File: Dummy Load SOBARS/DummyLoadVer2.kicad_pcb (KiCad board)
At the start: 2 copper layers, 57.2 x 47.6 mm, 22 parts, among them J2 Batt Monitor, J4 To Dummy Load 50 Ohms

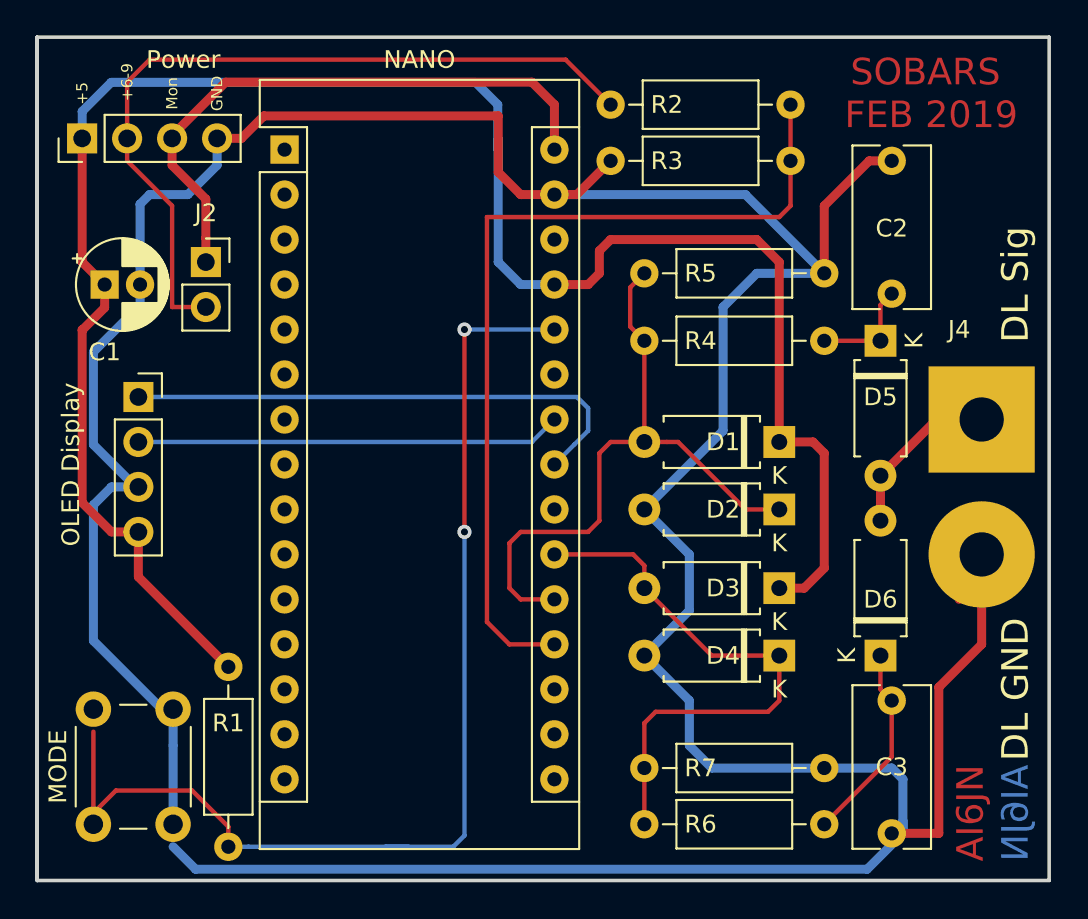
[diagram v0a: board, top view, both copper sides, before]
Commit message: Fix Mode Pin Digital Minor adjustments
Clean up some traces
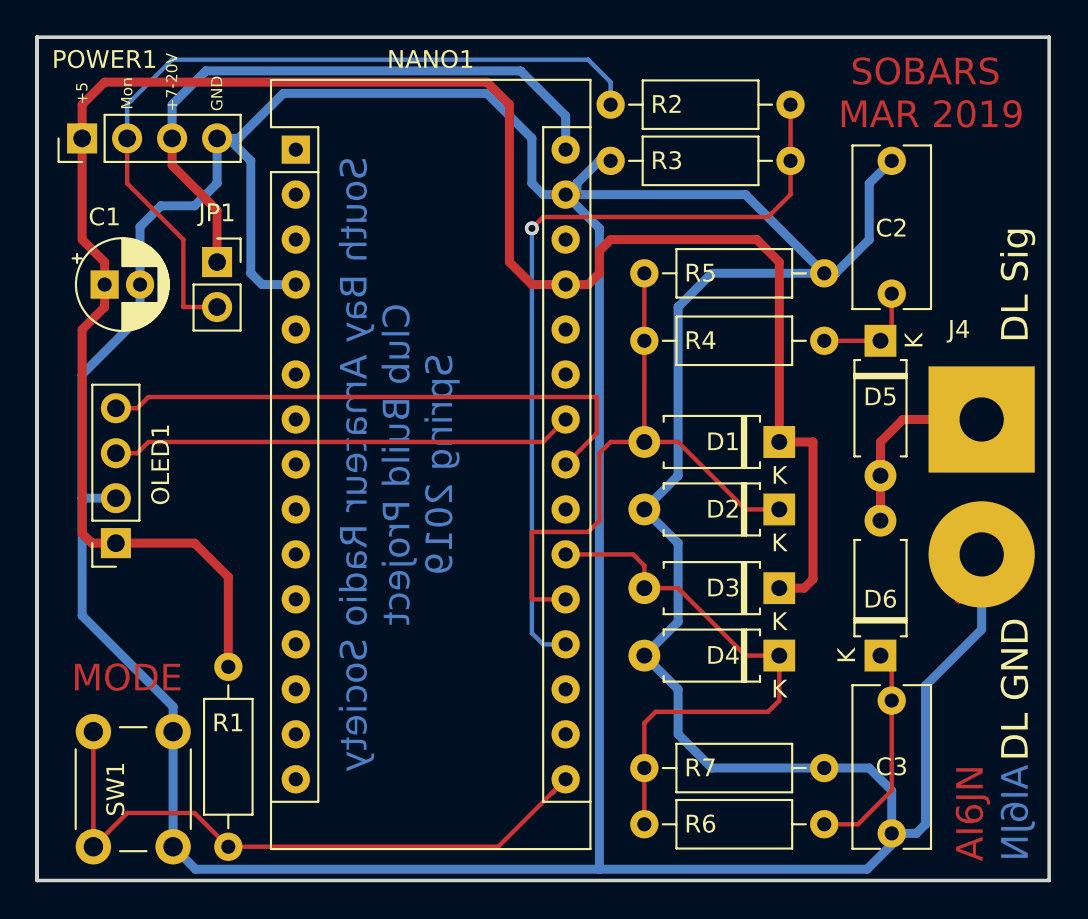
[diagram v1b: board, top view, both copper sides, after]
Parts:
- removed J2: Batt Monitor, Connector_PinSocket_2.54mm:PinSocket_1x02_P2.54mm_Vertical
- removed MODE: SW1, Button_Switch_THT:SW_PUSH_6mm
- removed NANO: Arduino_Nano_v3.x, Module:Arduino_Nano
- removed OLED Display: OLED Display 128X64, Connector_PinSocket_2.54mm:PinSocket_1x04_P2.54mm_Vertical
- removed Power: Power, Connector_PinHeader_2.54mm:PinHeader_1x04_P2.54mm_Vertical
- added JP1: Monitor Select, Connector_PinSocket_2.54mm:PinSocket_1x02_P2.54mm_Vertical, F.Cu at (76.8, 43.2)
- added NANO1: Arduino_Nano_v3.x, Module:Arduino_Nano, F.Cu at (81.3, 36.8)
- added OLED1: OLED Display 128X64, Connector_PinSocket_2.54mm:PinSocket_1x04_P2.54mm_Vertical, F.Cu at (71.1, 59.1)
- added POWER1: Power, Connector_PinHeader_2.54mm:PinHeader_1x04_P2.54mm_Vertical, F.Cu at (69.2, 36.2)
- added SW1: MODE, Button_Switch_THT:SW_PUSH_6mm, F.Cu at (69.8, 76.2)
- C1: value 4.7 -> 4.7uF
- C2, C3: value CAP -> 0.022uF
- J4: value To Dummy Load 50 Ohms -> To Dummy Load 50 Ohms
- R2: value 50K -> 22K
- R3: value 50K -> 6.8K
- R5: value 9K -> 8.2K
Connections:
- net Net-(D1-Pad2) renamed /LowADC
- net Net-(D3-Pad2) renamed /HighADC
- net Net-(D5-Pad2) renamed /LoadPositive
- net Net-(NANO1-Pad19) renamed /BattADC
- R1 pad 2: Net-(MODE1-Pad1) -> /MODE
- R2 pad 1: Net-(J1-Pad2) -> /BattMon
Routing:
- net Net-(MODE1-Pad1): track 63.2 -> 0.00 mm, vias 2 -> 0
- net GND: track 219.5 -> 270.3 mm
- net Net-(J1-Pad2): track 44.5 -> 0.00 mm
- net /BattMon: track 0.00 -> 44.2 mm
- net /MODE: track 0.00 -> 38.1 mm
- net /VinUnReg: track 0.00 -> 36.1 mm
- net Net-(J1-Pad3): track 33.8 -> 0.00 mm
- net /SDA: track 0.00 -> 32.0 mm
- net Net-(NANO1-Pad23): track 29.6 -> 0.00 mm
- net /SCL: track 0.00 -> 26.2 mm
- net Net-(NANO1-Pad24): track 24.7 -> 0.00 mm
- net /BattADC: track 50.3 -> 45.5 mm, vias 0 -> 1
- net /LowADC: track 36.9 -> 34.5 mm
- net +5V: track 112.2 -> 114.3 mm
- net /LoadPositive: track 9.57 -> 10.7 mm
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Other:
- rule pad_to_mask_clearance: 0.2 -> 0.1016
- board text added: "+7-20V"
- board text added: "MODE"
- board text added: "SOBARS MAR 2019"
- board text removed: "+6-9"
- board text removed: "SOBARS FEB 2019"
